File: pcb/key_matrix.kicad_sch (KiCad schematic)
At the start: 105 parts, among them SW1 SW_Push, SW10 SW_Push, SW11 SW_Push, SW12 SW_Push, SW13 SW_Push, SW14 SW_Push, SW15 SW_Push, SW16 SW_Push, SW17 SW_Push, SW18 SW_Push, SW19 SW_Push, SW2 SW_Push, SW20 SW_Push, SW21 SW_Push, SW22 SW_Push, SW23 SW_Push, SW24 SW_Push, SW25 SW_Push, SW26 SW_Push, SW27 SW_Push, SW28 SW_Push, SW29 SW_Push, SW3 SW_Push, SW30 SW_Push, SW31 SW_Push, SW32 SW_Push, SW33 SW_Push, SW34 SW_Push, SW35 SW_Push, SW36 SW_Push, SW37 SW_Push, SW38 SW_Push, SW39 SW_Push, SW4 SW_Push, SW40 SW_Push, SW41 SW_Push, SW42 SW_Push, SW43 SW_Push, SW44 SW_Push, SW45 SW_Push, SW5 SW_Push, SW54 RotaryEncoder_Switch, SW6 SW_Push, SW7 SW_Push, SW8 SW_Push, SW9 SW_Push

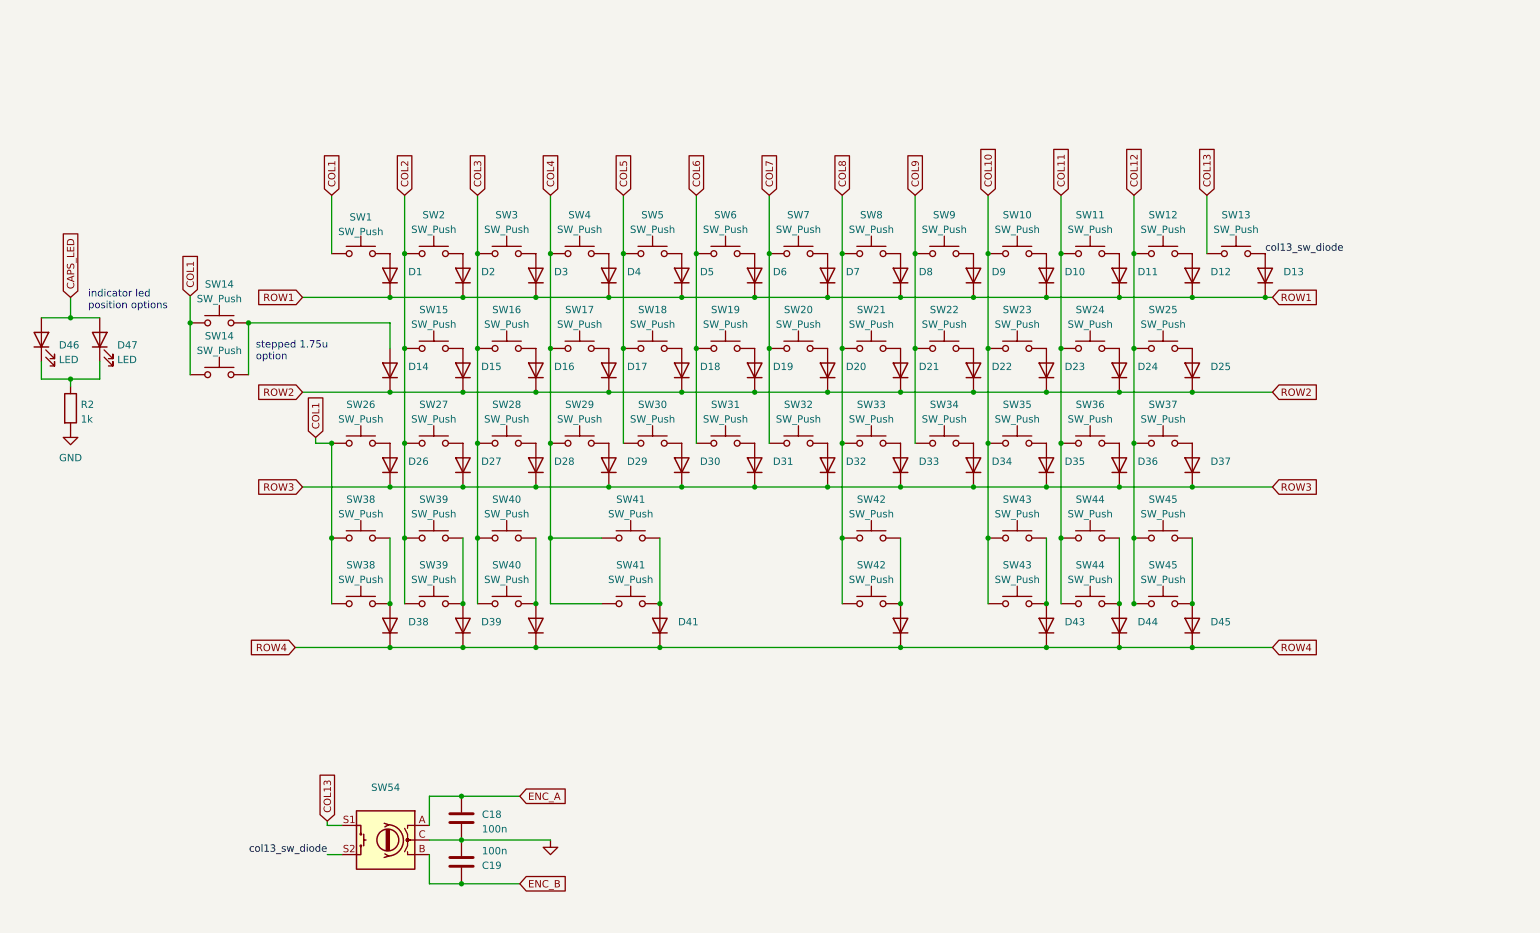
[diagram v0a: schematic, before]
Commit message: cleaned up schematic and added alps support
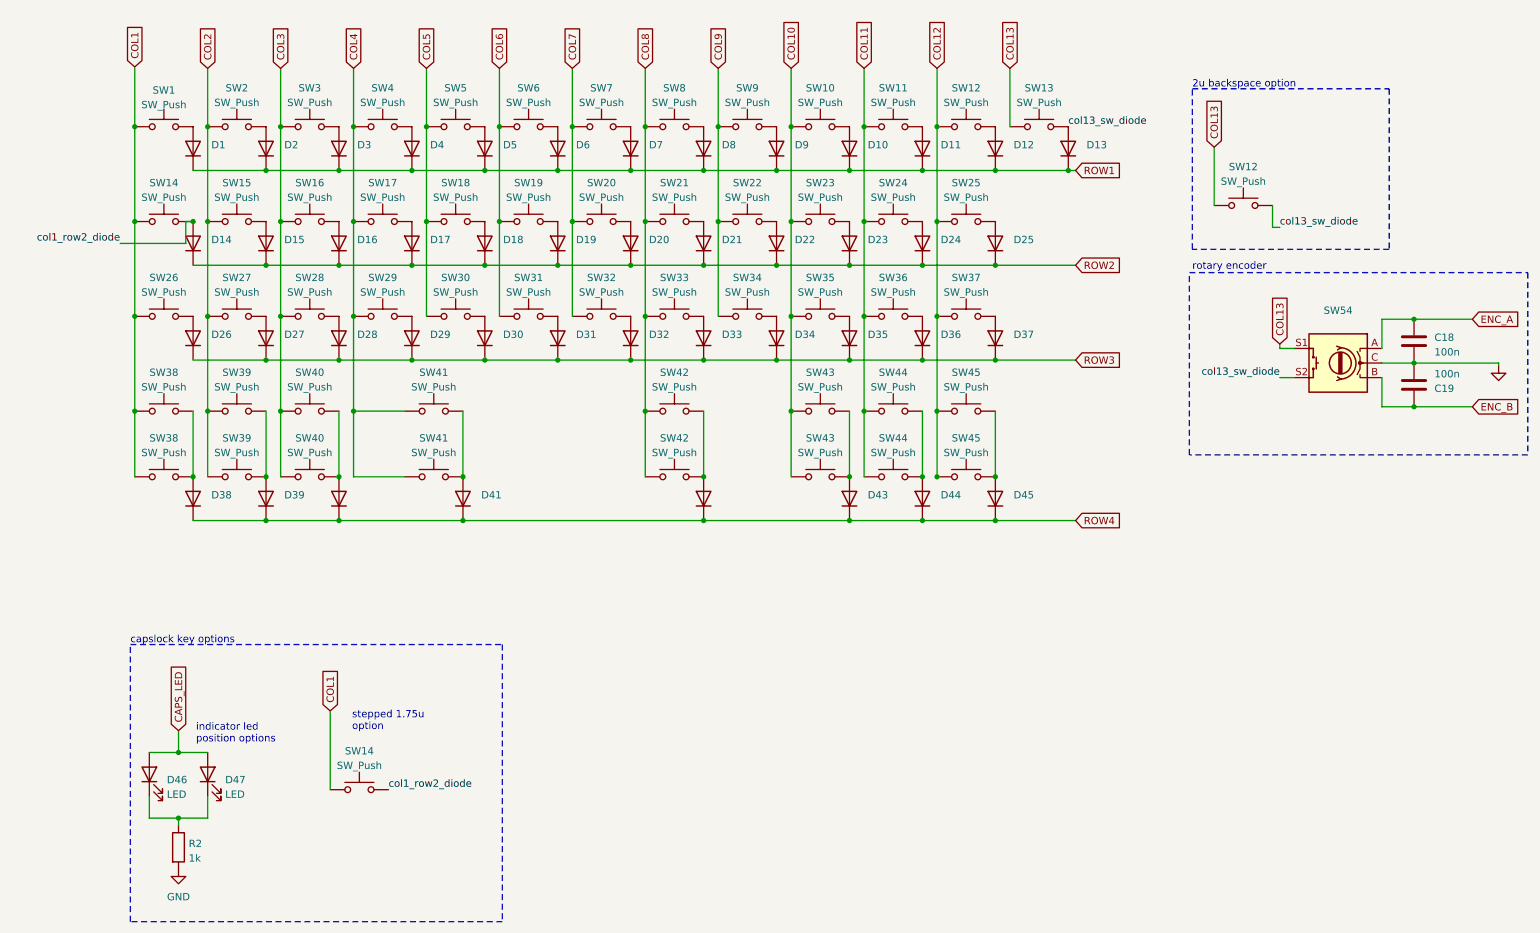
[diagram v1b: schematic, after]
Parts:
- added SW12: SW_Push, MX_Alps_Hybrid:MX-Alps-Hybrid-1U, symbol Switch:SW_Push
- SW1, SW38, SW40, SW43, SW45: footprint MX_Solderable:MX-Solderable-1.5U -> MX_Alps_Hybrid:MX-Alps-Hybrid-1.5U
- SW10, SW11, SW12, SW13, SW15, SW16, SW17, SW18, SW19, SW2, SW20, SW21, SW22, SW23, SW24, SW27, SW28, SW29, SW3, SW30, SW31, SW32, SW33, SW34, SW35, SW36, SW4, SW5, SW6, SW7, SW8, SW9: footprint MX_Solderable:MX-Solderable-1U -> MX_Alps_Hybrid:MX-Alps-Hybrid-1U
- SW14, SW25: footprint MX_Solderable:MX-Solderable-1.75U -> MX_Alps_Hybrid:MX-Alps-Hybrid-1.75U
- SW26: footprint MX_Solderable:MX-Solderable-2.25U -> MX_Alps_Hybrid:MX-Alps-Hybrid-2.25U
- SW37, SW38, SW39, SW40, SW43, SW44, SW45: footprint MX_Solderable:MX-Solderable-1.25U -> MX_Alps_Hybrid:MX-Alps-Hybrid-1.25U
- SW41, SW42: footprint MX_Solderable:MX-Solderable-3U-ReversedStabilizers -> MX_Alps_Hybrid:MX-Alps-Hybrid-3U-ReversedStabilizers
- SW41: footprint MX_Solderable:MX-Solderable-2.25U-ReversedStabilizers -> MX_Alps_Hybrid:MX-Alps-Hybrid-2.25U-ReversedStabilizers
- SW42: footprint MX_Solderable:MX-Solderable-2.75U-ReversedStabilizers -> MX_Alps_Hybrid:MX-Alps-Hybrid-2.75U-ReversedStabilizers
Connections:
- net COL13: now also SW12.2
- net col13_sw_diode: now also SW12.1
- net col1_row2_diode: now reaches D14.2 (A), SW14.1, SW14.2
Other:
- note added: "2u backspace option"
- note added: "capslock key options"
- note added: "rotary encoder"
- company: (none) -> sporkus
- title: (none) -> Bully2040 - MX/Alps
- moved on the sheet: C18, C19, D1, D10, D11, D12, D13, D14, D15, D16, D17, D18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
